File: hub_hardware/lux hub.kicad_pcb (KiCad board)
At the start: 4 copper layers, 99.7 x 49.5 mm, 109 parts, among them CON1 48V, CON2 USB-MINI-B, P1 CONN_4, P2 CONN_4, P3 CONN_4, P4 CONN_4, P5 CONN_4, P6 CONN_4, P7 CONN_4, Q1 DMP6023LE-13, SW1 BOOT, U1 3V3REG, U10 ISL83485IBZ, U11 2CH-TVS, U12 ISL83485IBZ, U13 2CH-TVS, U14 ISL83485IBZ, U15 2CH-TVS, U2 STM32F042-32, U3 4068, U4 ISL83485IBZ, U5 2CH-TVS, U6 ISL83485IBZ, U7 2CH-TVS, U8 ISL83485IBZ, U9 2CH-TVS

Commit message: Progress on v7 of led_strip_hardware; some lux utilities
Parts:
- added C13: 100n, SA0603, F.Cu at (42.4, 58.9)
- added C14: 100n, SA0603, F.Cu at (107.4, 63.2)
- added C15: 4u7, SA0603, F.Cu at (95.0, 73.9)
- moved R2 13.5 mm to (54.9, 63.5), turned to 270 degrees
- moved R50 6.35 mm to (122.9, 49.8)
- moved D1 6.10 mm to (116.8, 62.0)
- moved D15 4.19 mm to (118.9, 49.8), turned to 90 degrees
- moved R5 4.06 mm to (120.9, 62.0), turned to 90 degrees
- moved R4 2.03 mm to (122.9, 62.0)
- moved D16 1.91 mm to (116.8, 49.8), turned to 90 degrees
- moved R3 1.05 mm to (111.8, 63.2)
- moved C5 1.05 mm to (91.2, 73.9)
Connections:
- U2 pad 18: /TX_LED -> /sRX
- U2 pad 20: /sRX -> /TX_LED
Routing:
- net /sRX: track 12.5 -> 25.0 mm
- net (no net): track 0.25 -> 11.9 mm, vias 0 -> 9
- net Net-(C1-Pad1): track 31.3 -> 21.8 mm
- net /TX_LED: track 37.9 -> 28.6 mm
- net GND: track 127.3 -> 118.2 mm, vias 55 -> 48
- net /RX_LED: track 26.2 -> 32.7 mm
- net Net-(C1-Pad2): track 17.0 -> 11.1 mm, vias 2 -> 1
- net Net-(D1-Pad1): track 2.03 -> 7.86 mm
- net VCC: track 118.5 -> 123.9 mm, vias 21 -> 22
- net Net-(D16-Pad1): track 3.18 -> 8.10 mm
- net +48V: track 20.3 -> 22.2 mm, vias 2 -> 1
- net /Port6/LED: track 39.2 -> 38.0 mm
- net /Port3/DE: track 57.3 -> 58.3 mm
- net Net-(D15-Pad1): track 3.18 -> 2.30 mm
- net Net-(D2-Pad1): track 3.16 -> 2.57 mm
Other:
- board text added: "3V3"
- board text added: "48V"
- board text added: "EN"
- board text added: "Lux Hub"
- board text added: "Lux Hub rev 6 github.com/ervanalb/lux"
- board text added: "RX"
- board text added: "TX"
- board text removed: "LUX Router"
- board text removed: "LUX Router rev 5"

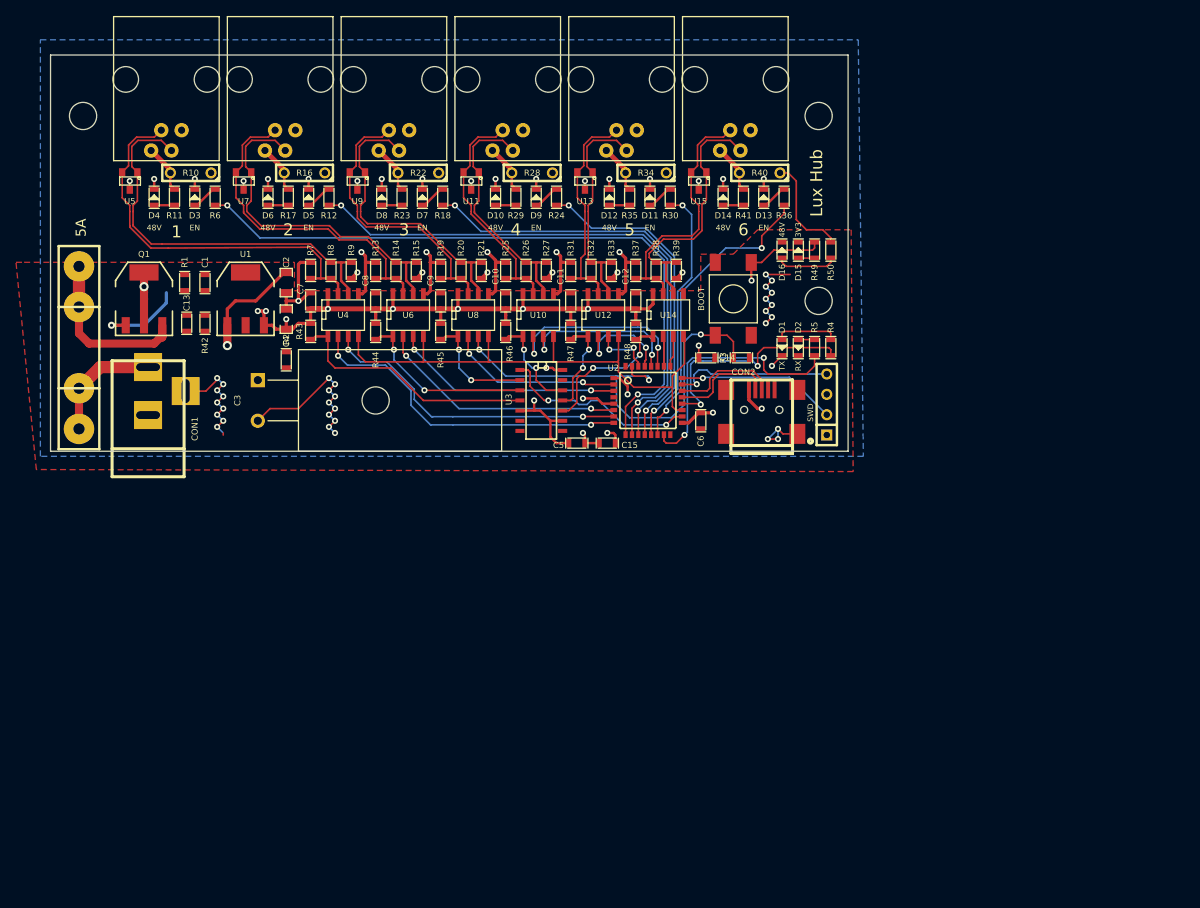
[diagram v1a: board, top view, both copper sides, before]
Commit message: Copper for the hub
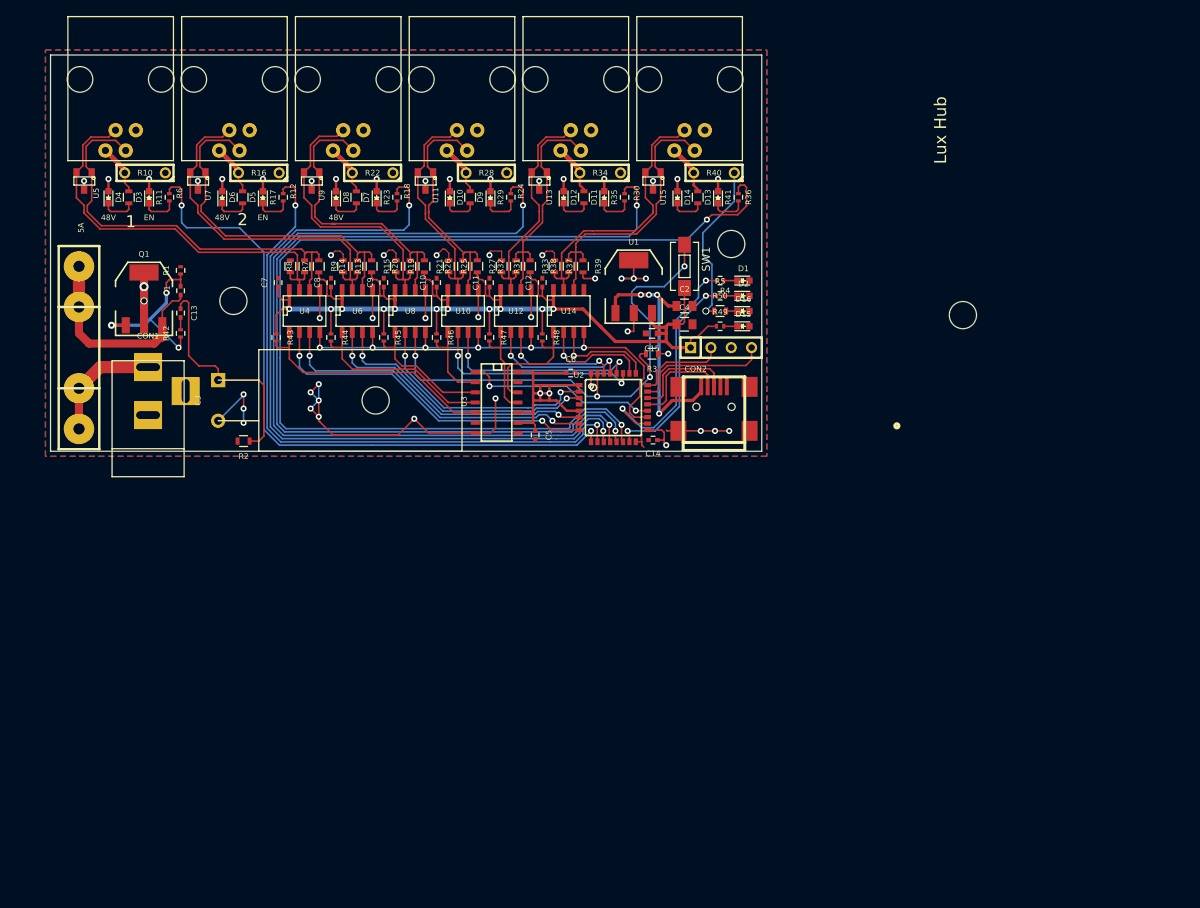
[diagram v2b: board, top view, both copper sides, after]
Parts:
- C1, C10, C11, C12, C13, C14, C5, C6, C7, C8, C9: footprint SA0603 -> Capacitors_SMD:C_0402
- C15: footprint SA0603 -> Capacitors_SMD:C_0603
- C2, C4: footprint SA0805 -> Capacitors_SMD:C_0805
- C3: footprint C2V8 -> Discret:C2V8
- CON1: footprint BARREL_JACK -> Connect:BARREL_JACK
- D1, D10, D11, D12, D13, D14, D15, D16, D2, D3, D4, D5, D6, D7, D8, D9: footprint SA0603_LED -> LEDs:LED_0603
- R1, R12, R18, R24, R30, R36, R4, R42, R43, R44, R45, R46, R47, R48, R49, R5, R6: footprint SA0603 -> Resistors_SMD:R_0402
- R11, R13, R14, R15, R17, R19, R2, R20, R21, R23, R25, R26, R27, R29, R3, R31, R32, R33, R35, R37, R38, R39, R41, R50, R7, R8, R9: footprint SA0603 -> Resistors_SMD:R_0603
- SW1: footprint TACT-SW-SMD -> Buttons_Switches_SMD:SW_SPST_EVQPE1
- moved HOLE 112.8 mm to (139.4, 57.9)
- moved HOLE 73.2 mm to (48.3, 56.1)
- moved C2 49.9 mm to (104.6, 56.8), turned to 0 degrees
- moved C4 49.8 mm to (104.6, 59.1), turned to 0 degrees
- moved U1 48.5 mm to (98.3, 54.4)
- moved HOLE 19.4 mm to (110.5, 49.0)
- moved C6 17.3 mm to (90.4, 65.2), turned to 0 degrees
- moved R4 16.2 mm to (109.1, 53.6), turned to 0 degrees
- moved R50 15.8 mm to (109.1, 57.4), turned to 0 degrees
- moved R49 15.2 mm to (109.1, 59.3), turned to 0 degrees
- moved P7 15.0 mm to (109.2, 62.0), turned to 0 degrees
- moved C15 14.8 mm to (100.6, 60.2)
- moved R5 13.5 mm to (109.1, 55.5), turned to 0 degrees
- moved U14 12.5 mm to (90.2, 57.4)
- moved C14 12.3 mm to (100.7, 73.5), turned to 180 degrees
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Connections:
- CON2 pad 6: GND -> (no net)
- SW1 pad 1: VCC -> /Port3/DE
- SW1 pad 2: Net-(SW1-Pad2) -> VCC
- U2 pad 18: /sRX -> /TX_LED
- U2 pad 20: /TX_LED -> /sRX
- U3 pad 10: /Port6/RX -> VCC
- U3 pad 12: /Port4/RX -> /Port6/RX
- U3 pad 2: /Port3/RX -> /Port4/RX
- U3 pad 3: /Port2/RX -> /Port3/RX
- U3 pad 4: /Port1/RX -> /Port2/RX
- U3 pad 5: VCC -> /Port1/RX
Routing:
- net /Port6/LED: track 38.0 -> 133.2 mm
- net /Port5/LED: track 32.9 -> 121.6 mm
- net /Port4/LED: track 41.6 -> 107.4 mm
- net VCC: track 123.9 -> 188.5 mm, vias 22 -> 15
- net Net-(C2-Pad1): track 97.3 -> 33.4 mm, vias 2 -> 4
- net /Port3/LED: track 55.8 -> 93.3 mm
- net +48V: track 22.2 -> 58.7 mm, vias 1 -> 3
- net (no net): track 11.9 -> 0.00 mm, vias 9 -> 0
- net Net-(C1-Pad2): track 11.1 -> 22.3 mm, vias 1 -> 3
- net /Port6/~RE: track 3.77 -> 13.7 mm, vias 0 -> 1
- net /Port2/LED: track 69.8 -> 79.0 mm
- net /Port6/DE: track 3.88 -> 12.8 mm, vias 0 -> 1
- net /SWCLK: track 20.1 -> 11.5 mm, vias 1 -> 0
- net /Port5/DE: track 7.43 -> 15.3 mm
- net /Port3/~RE: track 21.9 -> 29.7 mm
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- added copper zone on Inner1.Cu, net GND
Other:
- board size 99.7 x 49.5 mm -> 88.9 x 49.5 mm
- board text removed: "3V3"
- board text removed: "RX"
- board text removed: "SWD"
- board text removed: "TX"

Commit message: Hub gerbers; Reverting changes to lux API;
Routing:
- net VCC: track 188.5 -> 195.7 mm
- net GND: track 124.3 -> 119.2 mm, vias 47 -> 45
- net Net-(C2-Pad1): track 33.4 -> 29.6 mm, vias 4 -> 3
- net /Port3/DE: track 66.0 -> 64.6 mm
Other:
- board text added: "RX"
- board text added: "TX"
- board text added: "VCC"
- board text added: "Zach Banks zjbanks@gmail.com"
- board text removed: "Lux Hub"
- board text removed: "Zach Banks zbanks@mit.edu"

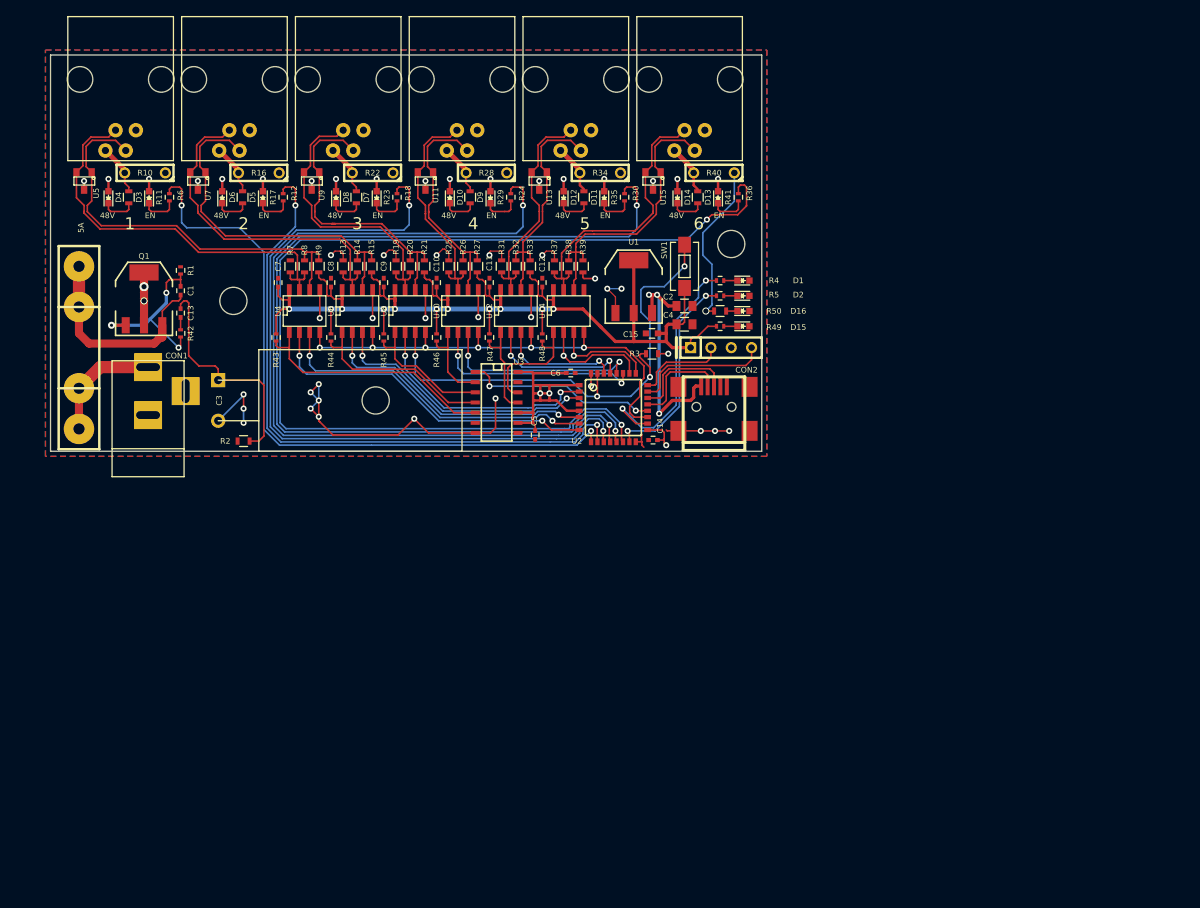
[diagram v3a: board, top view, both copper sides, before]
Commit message: WIP Lux Hub v7
* Replace PTCs with current-limiting circuit
* Widen board and add 4x2mm mounting holes
* TODO: Rearrange some components on the edges
* TODO: Check silkscreen (esp. LEDs)
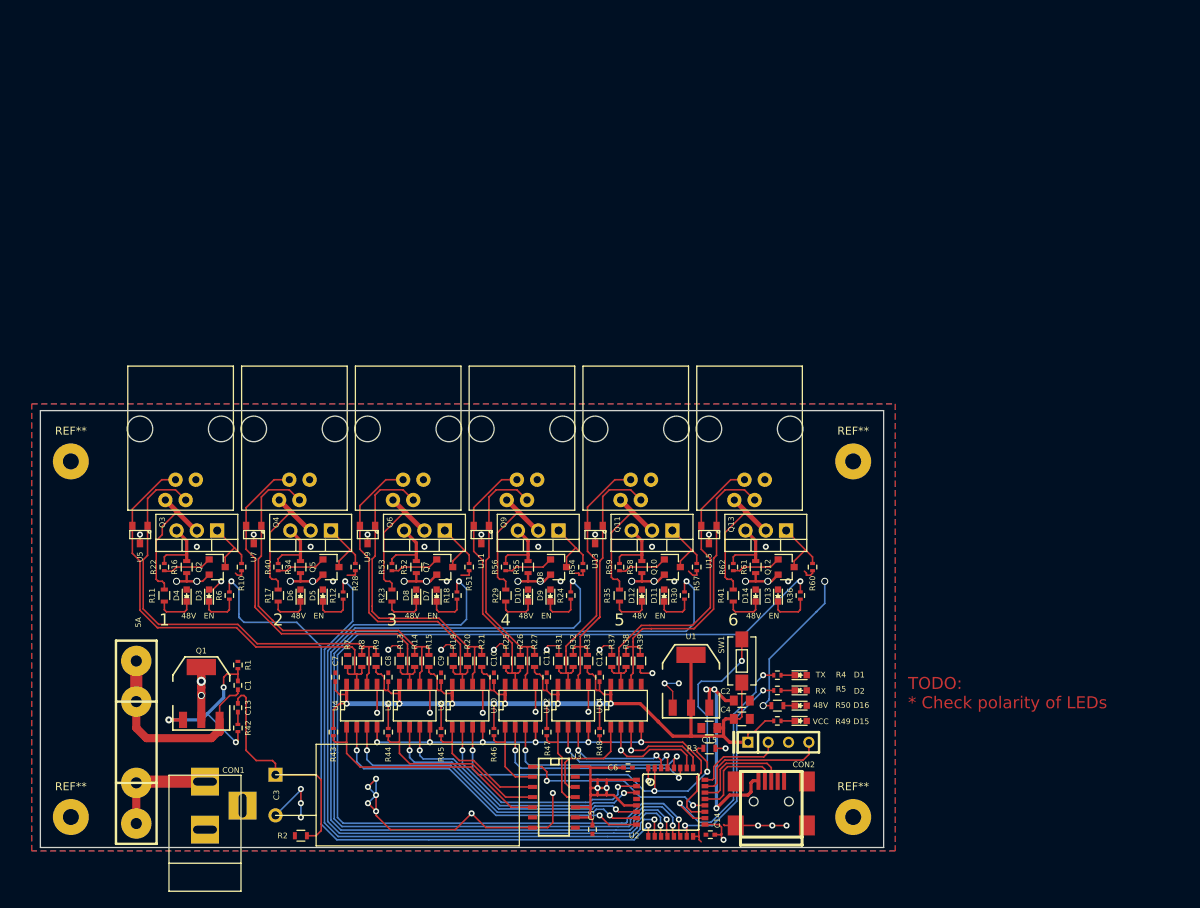
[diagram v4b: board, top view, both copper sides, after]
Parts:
- removed HOLE (x4): VAL**, HOLE
- added Q10: BC856BLT, TO_SOT_Packages_SMD:SOT-23, F.Cu at (103.1, 89.4)
- added Q11: BTX54CTU, TO_SOT_Packages_THT:TO-220-3_Vertical, F.Cu at (103.1, 84.8)
- added Q12: BC856BLT, TO_SOT_Packages_SMD:SOT-23, F.Cu at (117.3, 89.4)
- added Q13: BTX54CTU, TO_SOT_Packages_THT:TO-220-3_Vertical, F.Cu at (117.3, 84.8)
- added Q2: BC856BLT, TO_SOT_Packages_SMD:SOT-23, F.Cu at (46.2, 89.4)
- added Q3: BTX54CTU, TO_SOT_Packages_THT:TO-220-3_Vertical, F.Cu at (46.2, 84.8)
- added Q4: BC856BLT, TO_SOT_Packages_SMD:SOT-23, F.Cu at (60.5, 89.4)
- added Q5: BTX54CTU, TO_SOT_Packages_THT:TO-220-3_Vertical, F.Cu at (60.5, 84.8)
- added Q6: BC856BLT, TO_SOT_Packages_SMD:SOT-23, F.Cu at (74.7, 89.4)
- added Q7: BTX54CTU, TO_SOT_Packages_THT:TO-220-3_Vertical, F.Cu at (74.7, 84.8)
- added Q8: BC856BLT, TO_SOT_Packages_SMD:SOT-23, F.Cu at (88.9, 89.4)
- added Q9: BTX54CTU, TO_SOT_Packages_THT:TO-220-3_Vertical, F.Cu at (88.9, 84.8)
- added R51: 10K, Resistors_SMD:R_0402, F.Cu at (77.7, 89.4)
- added R52: 2, Resistors_SMD:R_0603, F.Cu at (71.1, 89.4)
- added R53: 10K, Resistors_SMD:R_0402, F.Cu at (68.1, 89.4)
- added R54: 10K, Resistors_SMD:R_0402, F.Cu at (91.9, 89.4)
- added R55: 2, Resistors_SMD:R_0603, F.Cu at (85.1, 89.4)
- added R56: 10K, Resistors_SMD:R_0402, F.Cu at (82.3, 89.4)
- added R57: 10K, Resistors_SMD:R_0402, F.Cu at (106.2, 89.4)
- added R58: 2, Resistors_SMD:R_0603, F.Cu at (99.3, 89.4)
- added R59: 10K, Resistors_SMD:R_0402, F.Cu at (96.5, 89.4)
- added R60: 10K, Resistors_SMD:R_0402, F.Cu at (120.7, 89.4)
- added R61: 2, Resistors_SMD:R_0603, F.Cu at (113.5, 89.4)
- added R62: 10K, Resistors_SMD:R_0402, F.Cu at (110.7, 89.4)
- added REF**: SolderWirePad_single_2mmDrill, Wire_Pads:SolderWirePad_single_2mmDrill, F.Cu at (27.9, 120.7)
- added REF**: SolderWirePad_single_2mmDrill, Wire_Pads:SolderWirePad_single_2mmDrill, F.Cu at (27.9, 76.2)
- added REF**: SolderWirePad_single_2mmDrill, Wire_Pads:SolderWirePad_single_2mmDrill, F.Cu at (125.7, 76.2)
- added REF**: SolderWirePad_single_2mmDrill, Wire_Pads:SolderWirePad_single_2mmDrill, F.Cu at (125.7, 120.7)
- C15: footprint Capacitors_SMD:C_0603 -> Capacitors_SMD:C_0805
- R10, R22, R28, R40: value PTC -> 10K; footprint C2 -> Resistors_SMD:R_0402
- R16, R34: value PTC -> 2; footprint C2 -> Resistors_SMD:R_0603
- moved R40 73.5 mm to (53.8, 89.4), turned to 90 degrees
- moved R34 61.9 mm to (56.6, 89.4), turned to 90 degrees
- moved R22 55.7 mm to (39.6, 89.4), turned to 90 degrees
- moved CON1 52.3 mm to (44.7, 122.4)
- moved R28 51.9 mm to (63.5, 89.4), turned to 90 degrees
- moved D8 50.8 mm to (71.1, 93.0)
- moved D10 50.7 mm to (85.1, 93.0)
- moved D12 50.7 mm to (99.3, 93.0)
- moved D14 50.7 mm to (113.5, 93.0)
- moved D4 50.7 mm to (42.4, 93.0)
- moved D6 50.7 mm to (56.6, 93.0)
- moved R10 50.7 mm to (49.3, 89.4), turned to 90 degrees
- moved R36 50.4 mm to (119.1, 93.0)
- moved D11 50.3 mm to (102.1, 93.0)
- moved D13 50.3 mm to (116.3, 93.0)
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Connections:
- net /Port1/DE renamed /DE1
- net /Port1/LED renamed /LED1
- net /Port1/RX renamed /RX1
- net /Port1/TX renamed /TX
- net /Port1/~RE renamed /RE1
- net /Port2/DE renamed /DE2
- net /Port2/LED renamed /LED2
- net /Port2/RX renamed /RX2
- net /Port2/~RE renamed /RE2
- net /Port3/DE renamed /DE3
- net /Port3/LED renamed /LED3
- net /Port3/RX renamed /RX3
- net /Port3/~RE renamed /RE3
- net /Port4/DE renamed /DE4
- net /Port4/LED renamed /LED4
- net /Port4/RX renamed /RX4
- net /Port4/~RE renamed /RE4
- net /Port5/DE renamed /DE5
- net /Port5/LED renamed /LED5
- net /Port5/RX renamed /RX5
- net /Port5/~RE renamed /RE5
- net /Port6/DE renamed /DE6
- net /Port6/LED renamed /LED6
- net /Port6/RX renamed /RX6
- net /Port6/~RE renamed /RE6
- CON2 pad 4: Net-(CON2-Pad4) -> (no net)
- R10 pad 1: +48V -> GND
- R10 pad 2: /Port1/P48 -> Net-(Q2-Pad3)
- R16 pad 2: /Port2/P48 -> Net-(Q3-Pad3)
- R22 pad 1: +48V -> Net-(Q2-Pad1)
- R22 pad 2: /Port3/P48 -> Net-(Q3-Pad3)
- R28 pad 1: +48V -> GND
- R28 pad 2: /Port4/P48 -> Net-(Q4-Pad3)
- R34 pad 2: /Port5/P48 -> Net-(Q5-Pad3)
- R40 pad 1: +48V -> Net-(Q4-Pad1)
- R40 pad 2: /Port6/P48 -> Net-(Q5-Pad3)
- U3 pad 13: Net-(U3-Pad13) -> (no net)
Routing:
- net +48V: track 58.7 -> 90.5 mm, vias 3 -> 16
- net /Port6/P48: track 6.05 -> 17.0 mm
- net /Port5/P48: track 6.05 -> 17.0 mm
- net /Port2/P48: track 6.30 -> 17.3 mm
- net /Port3/P48: track 6.30 -> 17.1 mm
- net /Port1/P48: track 6.30 -> 17.0 mm
- net /Port4/P48: track 6.30 -> 17.0 mm
- net Net-(Q10-Pad3): track 0.00 -> 8.31 mm
- net Net-(Q7-Pad3): track 0.00 -> 8.28 mm
- net Net-(Q2-Pad3): track 0.00 -> 8.28 mm
- net Net-(Q8-Pad3): track 0.00 -> 8.28 mm
- net Net-(Q12-Pad3): track 0.00 -> 8.23 mm
- net Net-(Q4-Pad3): track 0.00 -> 8.13 mm
- net Net-(Q6-Pad3): track 0.00 -> 8.13 mm
- net Net-(Q9-Pad3): track 0.00 -> 8.07 mm
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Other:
- board size 88.9 x 49.5 mm -> 105.4 x 54.6 mm
- board text added: "Lux Hub rev 7 github.com/ervanalb/lux"
- board text added: "TODO: * Check polarity of LEDs"
- board text removed: "Lux Hub rev 6 github.com/ervanalb/lux"
